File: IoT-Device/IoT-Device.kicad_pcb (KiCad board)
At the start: 4 copper layers, 100 x 70 mm, 64 parts, among them J1 USB-C, J2 Conn_01x02, J3 SWD, SW1 RESET, SW2 BOOT_MODE, SW3 B1, SW4 B2, U1 BD33GA5WEFJ, U2 STM32U585VI, U3 BQ24074RGT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

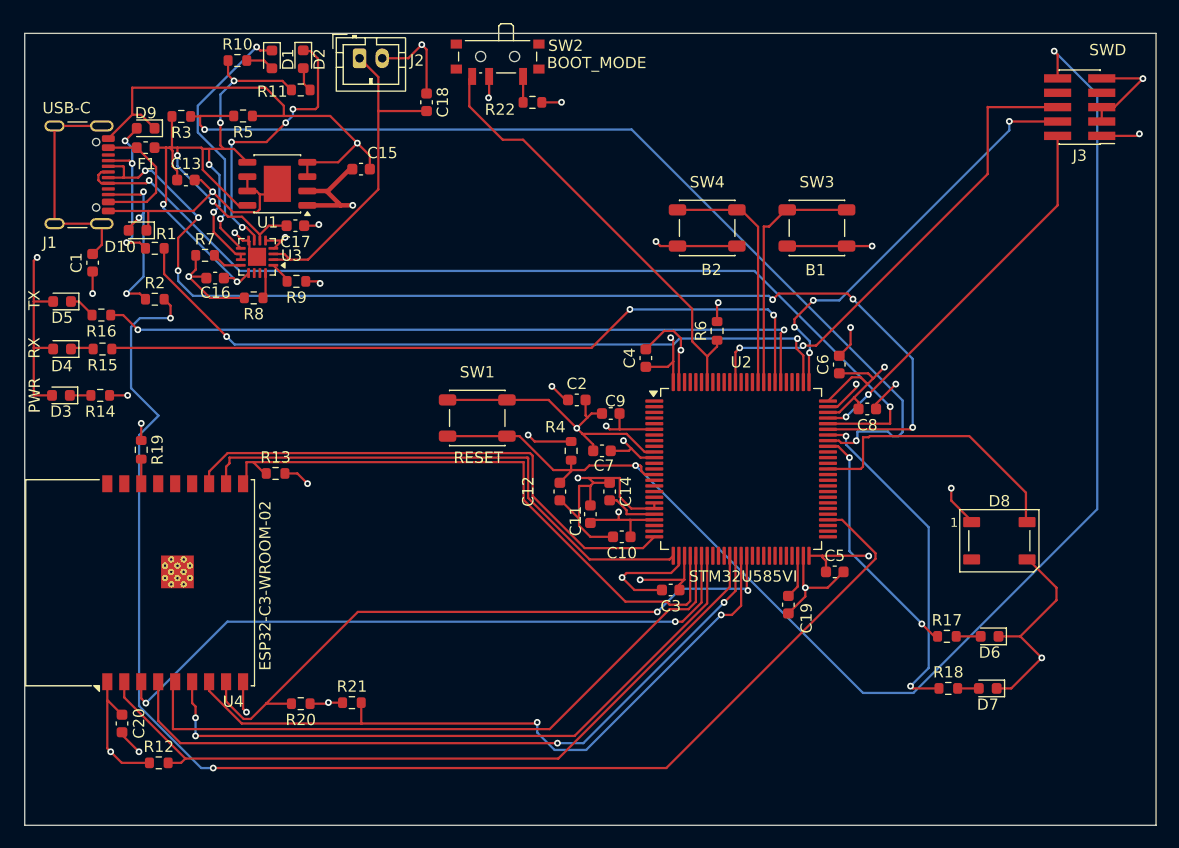
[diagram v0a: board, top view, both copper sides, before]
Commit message: add microSD card slot
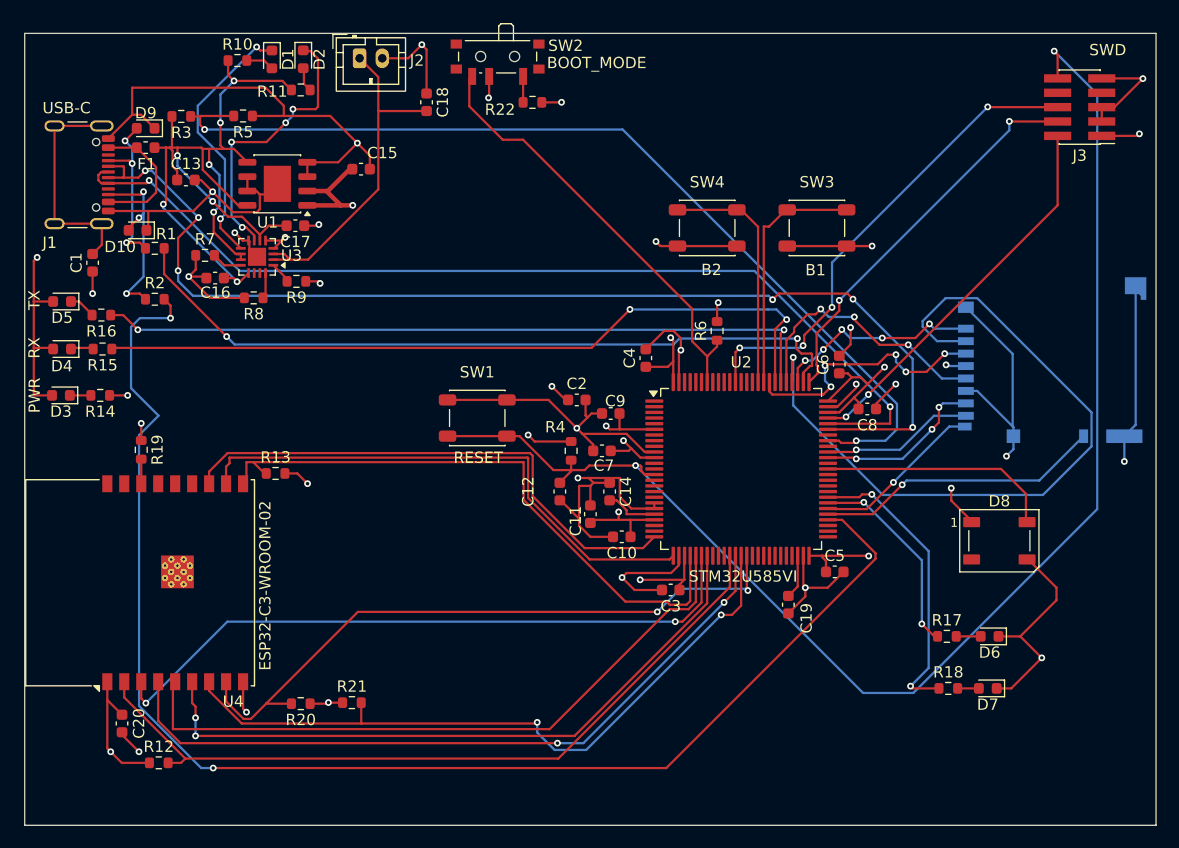
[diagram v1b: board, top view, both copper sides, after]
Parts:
- added J4: Micro_SD_Card_Det2, Connector_Card:microSD_HC_Hirose_DM3BT-DSF-PEJS, B.Cu at (115.8, 48.9)
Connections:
- U2 pad 55: unconnected-(U2-PD8-Pad55) -> /SD_DET_A
- U2 pad 56: unconnected-(U2-PD9-Pad56) -> /SD_DET_B
- U2 pad 57: unconnected-(U2-PD10-Pad57) -> /LED1
- U2 pad 58: unconnected-(U2-PD11-Pad58) -> /LED2
- U2 pad 65: unconnected-(U2-PC8-Pad65) -> /SDMMC1_D0
- U2 pad 66: unconnected-(U2-PC9-Pad66) -> /SDMMC1_D1
- U2 pad 67: /LED1 -> unconnected-(U2-PA8-Pad67)
- U2 pad 69: /LED2 -> unconnected-(U2-PA10-Pad69)
- U2 pad 78: unconnected-(U2-PC10-Pad78) -> /SDMMC1_D2
- U2 pad 79: unconnected-(U2-PC11-Pad79) -> /SDMMC1_D3
- U2 pad 80: unconnected-(U2-PC12-Pad80) -> /SDMMC1_CK
- U2 pad 83: unconnected-(U2-PD2-Pad83) -> /SDMMC1_CMD
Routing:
- net /SDMMC1_D3: track 0.00 -> 65.7 mm, vias 0 -> 1
- net GND: track 236.7 -> 273.3 mm, vias 26 -> 28
- net /SD_DET_A: track 0.00 -> 25.5 mm, vias 0 -> 1
- net /SDMMC1_CK: track 0.00 -> 23.6 mm, vias 0 -> 3
- net /SDMMC1_CMD: track 0.00 -> 23.3 mm, vias 0 -> 5
- net /SDMMC1_D2: track 0.00 -> 18.6 mm, vias 0 -> 5
- net /SDMMC1_D0: track 0.00 -> 15.1 mm, vias 0 -> 3
- net /SD_DET_B: track 0.00 -> 14.5 mm, vias 0 -> 1
- net /SDMMC1_D1: track 0.00 -> 13.5 mm, vias 0 -> 1
- net /NEOPIXEL: track 24.7 -> 20.7 mm
- net /LED2: track 30.3 -> 26.5 mm
- net /LED1: track 21.2 -> 17.7 mm
- net /SWCLK: track 37.2 -> 34.7 mm, vias 4 -> 2
- net /MCU_VBUS: track 87.5 -> 85.5 mm
- net /RX_LED: track 66.1 -> 67.5 mm
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
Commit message: fix STM32<->ESP32-C3 UART communication, update labels on shcematics
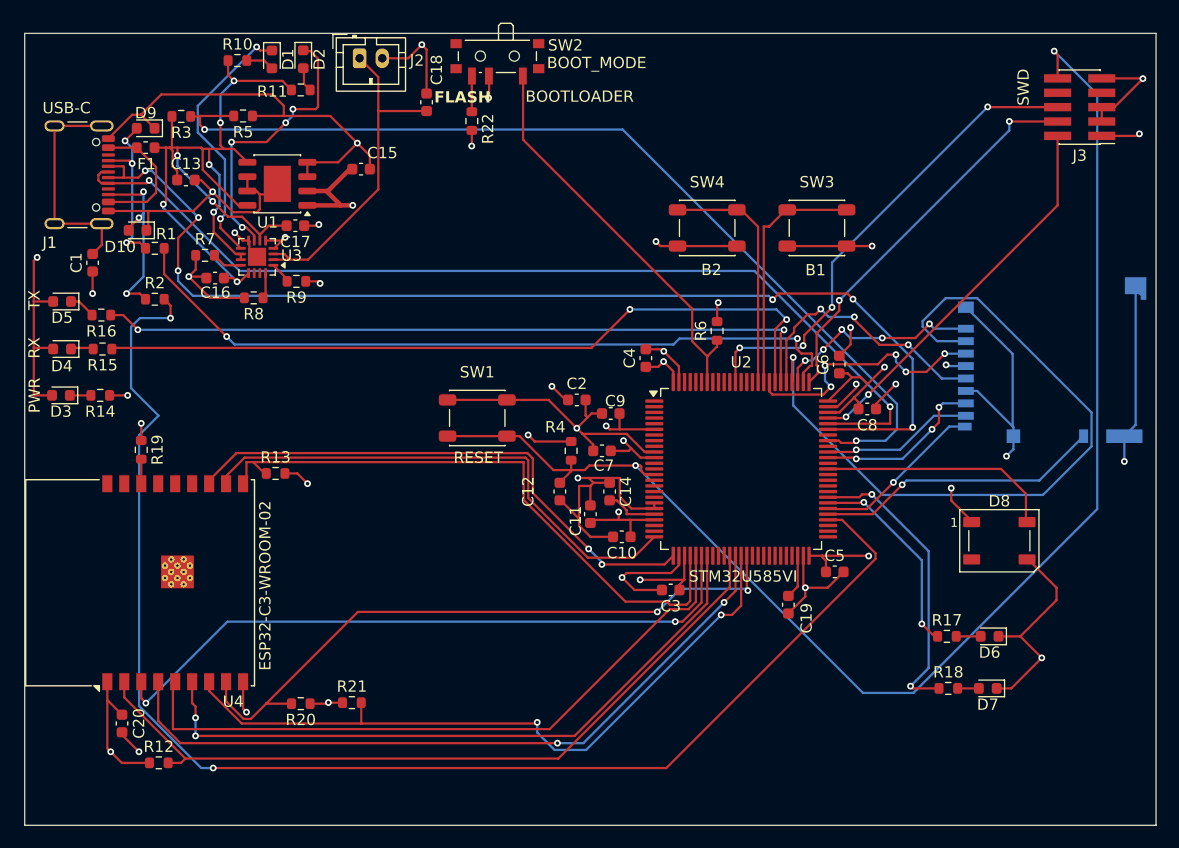
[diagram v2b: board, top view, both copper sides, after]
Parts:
- D3: value PWR -> LED
- D4: value RX -> LED
- D5: value TX -> LED
- J1: value USB-C -> USB_C_Receptacle_USB2.0_16P
- J3: value SWD -> Conn_ARM_JTAG_SWD_10
- SW2: value BOOT_MODE -> SW_SPDT
- SW3: value B1 -> SW_Push
- SW4: value B2 -> SW_Push
- moved R22 5.61 mm to (64.5, 27.8), turned to -90 degrees
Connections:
- R22 pad 1: Net-(SW2-A) -> Net-(SW2-C)
- SW2 pad 1: Net-(SW2-A) -> /BOOT0
- SW2 pad 3: /BOOT0 -> Net-(SW2-C)
- U4 pad 11: /USART2_RX -> /USART2_TX
- U4 pad 12: /USART2_TX -> /USART2_RX
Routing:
- net GND: track 273.3 -> 267.2 mm
- net Net-(SW2-C): track 0.00 -> 3.13 mm
- net /BOOT0: track 38.7 -> 35.5 mm
- net +3.3V: track 117.4 -> 114.6 mm
- net Net-(SW2-A): track 2.30 -> 0.00 mm
- net /USART2_TX: track 47.1 -> 45.6 mm
- net /USART2_RX: track 47.7 -> 48.6 mm, vias 0 -> 2
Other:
- board text added: "BOOTLOADER"
- board text added: "FLASH"
